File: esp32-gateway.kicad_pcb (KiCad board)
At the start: 2 copper layers, 55 x 95 mm, 49 parts, among them J1 USB_B_Micro, J2 Button Connector, J3 Ext LED header, J4 Conn_Coaxial, J5 Header Left, J6 Header Right, Q1 Q_NPN_BEC, Q2 Q_NPN_BEC, SW1 SW_RESET, SW2 SW_INCLUSION, SW3 SW_GEN1, SW4 SW_BOOT, U1 RFM69HCW, U2 ESP-WROOM-32, U3 AMS1117-3.3, U4 AMS1117-3.3, U5 RFM69CW, U6 NRF24L01_Breakout, U7 RFM69(H)W, U8 CH340C

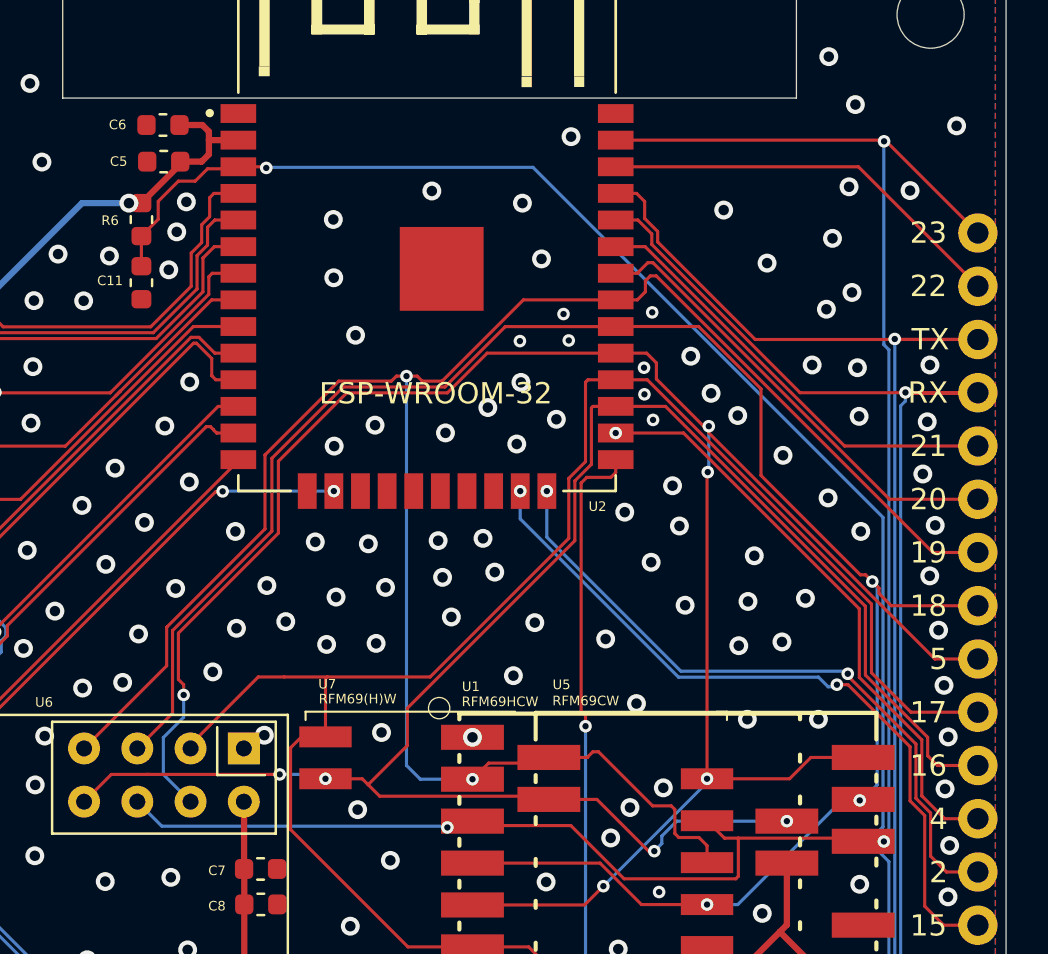
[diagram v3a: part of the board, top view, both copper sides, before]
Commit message: Added I2C breakout header
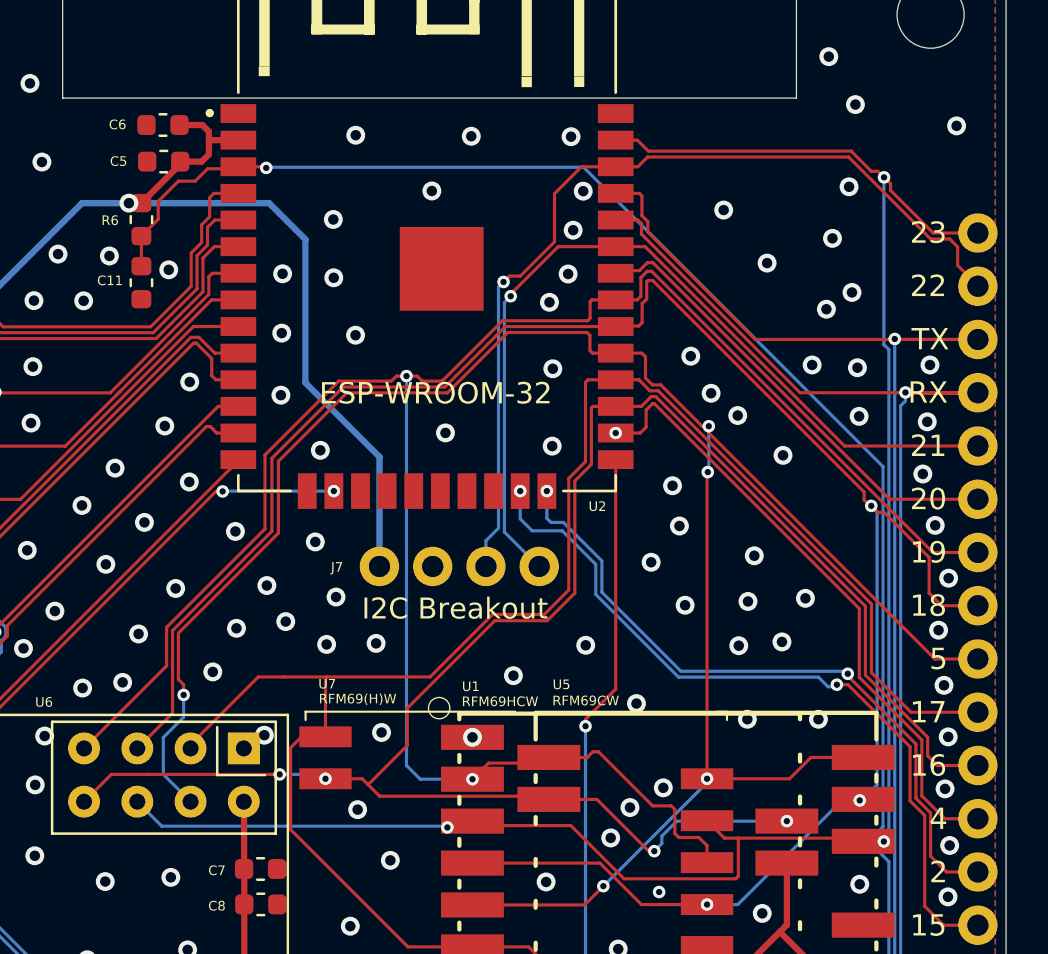
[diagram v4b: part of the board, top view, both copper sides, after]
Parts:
- added J7: I2C Breakout, Sparkfun Connectors:1X04_NO_SILK, F.Cu at (140.1, 94.9)
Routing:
- net LEDB: track 172.0 -> 198.2 mm
- net IO22: track 19.6 -> 43.4 mm, vias 0 -> 1
- net IO21: track 21.2 -> 41.0 mm, vias 0 -> 1
- net IO18: track 94.1 -> 99.2 mm
- net IO16: track 86.9 -> 88.8 mm
- net IO4: track 28.6 -> 30.2 mm
- net IO23: track 91.6 -> 90.0 mm
- net CE-RST: track 81.0 -> 82.5 mm
- net EN: track 115.9 -> 117.4 mm
- net IO5: track 100.3 -> 101.7 mm
- net IO19: track 98.2 -> 99.0 mm
- net IO0: track 69.9 -> 69.1 mm
- net IO15: track 36.1 -> 36.9 mm
- net GND: vias 195 -> 178

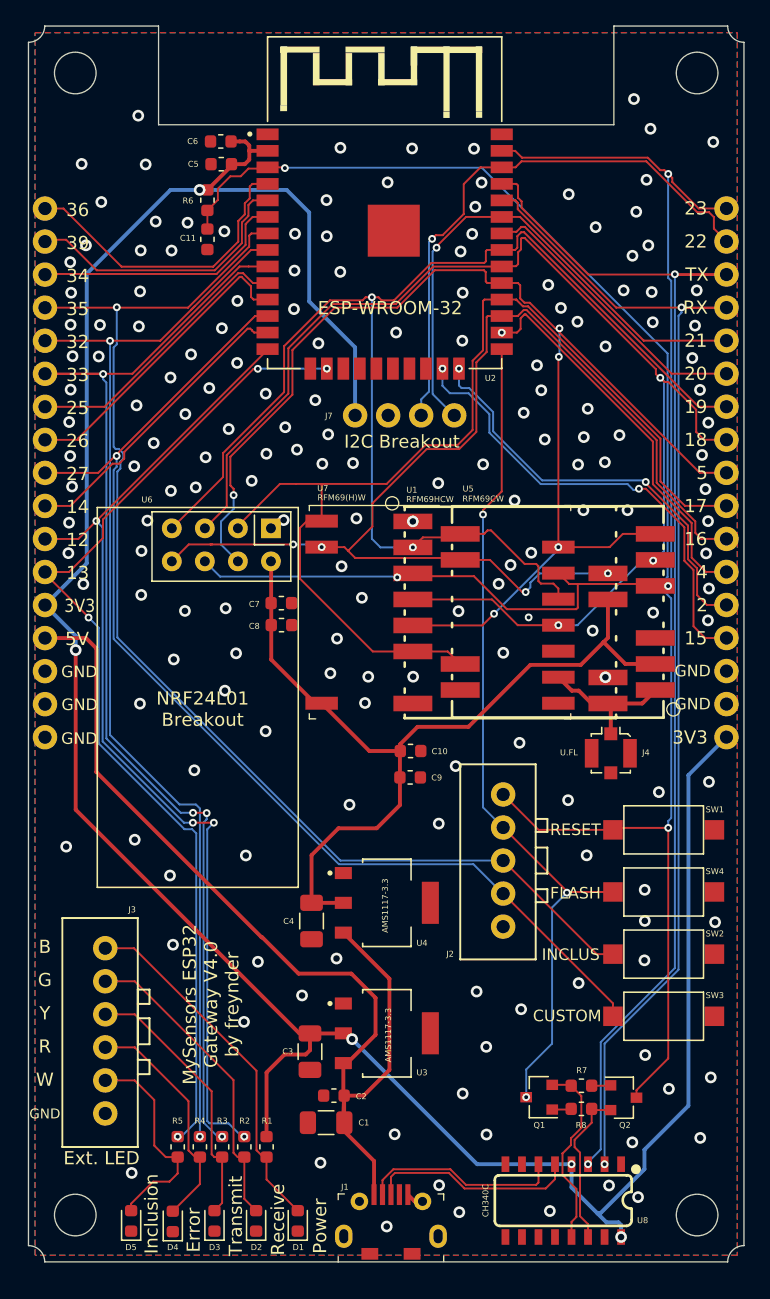
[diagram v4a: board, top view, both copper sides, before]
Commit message: Added Breakout for RXB6 433Mhz RF receiver
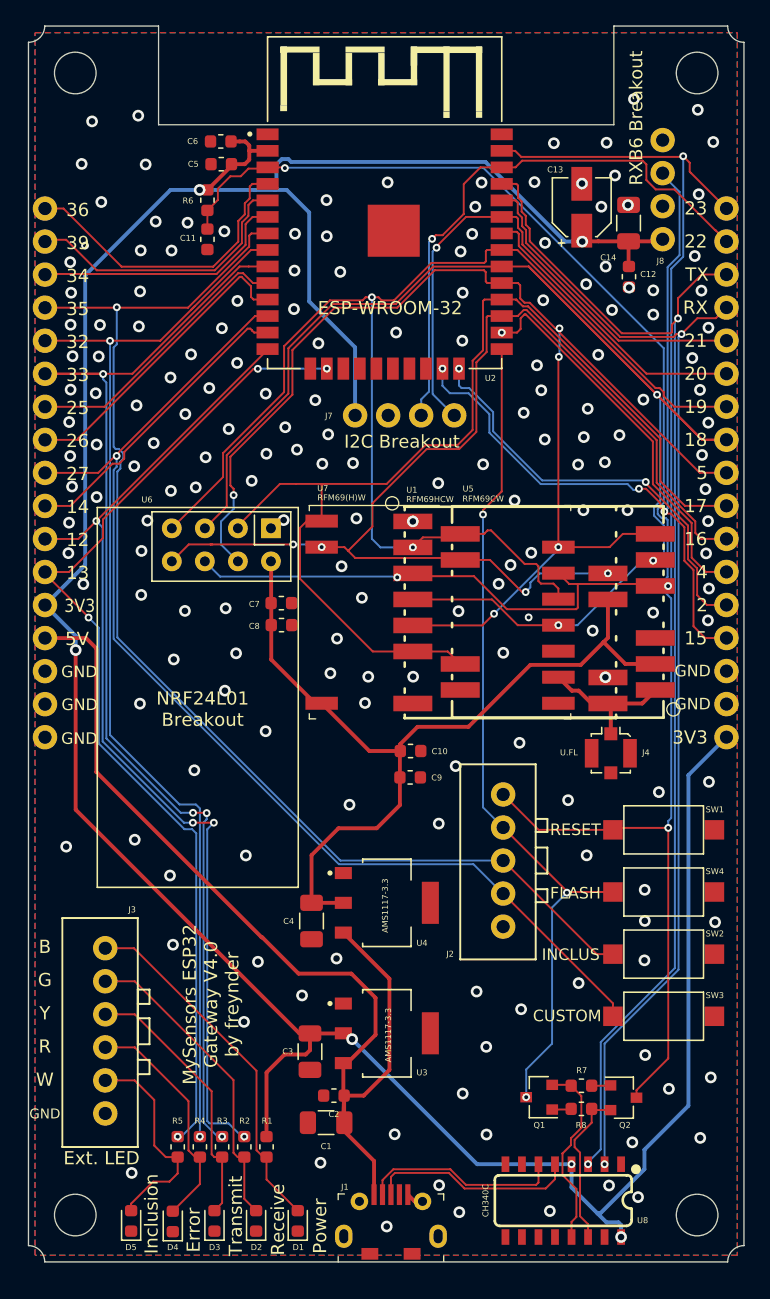
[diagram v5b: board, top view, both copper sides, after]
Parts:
- added C12: 10uF, Capacitor_SMD:C_1206_3216Metric, F.Cu at (161.1, 80.2)
- added C13: 0.47uF, Capacitor_SMD:CP_Elec_4x5.4, F.Cu at (157.5, 78.9)
- added C2: 0.1uF, Capacitor_SMD:C_0603_1608Metric, F.Cu at (138.5, 147.2)
- added J8: RXB6 Breakout, Sparkfun Connectors:1X04_NO_SILK, F.Cu at (163.8, 81.4)
- J4: value Conn_Coaxial -> u.FL
- moved C14 66.9 mm to (161.2, 84.3), turned to 270 degrees
- renumbered C2 to C14
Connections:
- C14 pad 1: +5V -> LEDB
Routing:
- net LEDB: track 198.2 -> 234.7 mm, vias 5 -> 6
- net IO15: track 36.9 -> 64.2 mm, vias 2 -> 3
- net IO18: track 99.2 -> 115.4 mm
- net ESPRX: track 92.8 -> 90.3 mm
- net IO23: track 90.0 -> 91.9 mm
- net IO19: track 99.0 -> 97.6 mm
- net ESPTX: track 96.2 -> 95.0 mm
- net IO21: track 41.0 -> 41.9 mm
- net EN: track 117.4 -> 118.0 mm
- net GND: vias 178 -> 185

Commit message: Added pullup pins for I2C
Please note that some breakout boards come with pullups included. It is
advisable to desolder those or not include the pullup pins on the board.
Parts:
- added R10: 4.7K, Resistor_SMD:R_0603_1608Metric, F.Cu at (146.5, 98.2)
- added R9: 4.7K, Resistor_SMD:R_0603_1608Metric, F.Cu at (143.1, 98.2)
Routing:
- net LEDB: track 234.7 -> 244.2 mm
- net IO22: track 43.7 -> 47.4 mm
- net IO21: track 41.9 -> 45.4 mm
- net CE-RST: track 82.5 -> 83.8 mm
- net IO16: track 88.8 -> 90.0 mm
- net GND: vias 185 -> 184
